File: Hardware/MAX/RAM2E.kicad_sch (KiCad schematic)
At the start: 61 parts, among them J1 AppleIIeAux, J2 JTAG, J3 C14M, U1 EPM240T100, U2 W9812G6KH-6, U3 74LVC245APW, U4 74LVC245APW, U5 74LVC245APW, U6 74AHCT245PW, U7 74AHCT245PW, U8 XC6206P332MR, U9 AP2127K-1.8TRG1

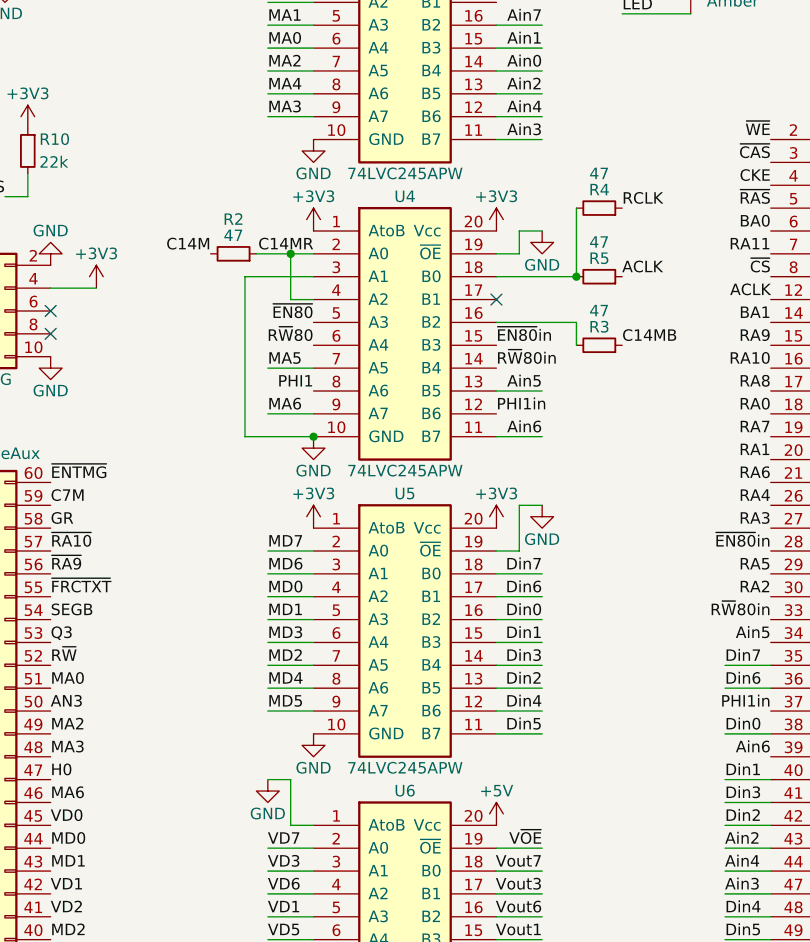
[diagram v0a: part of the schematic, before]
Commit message: Change BOM to separate U4 from U3 and U5
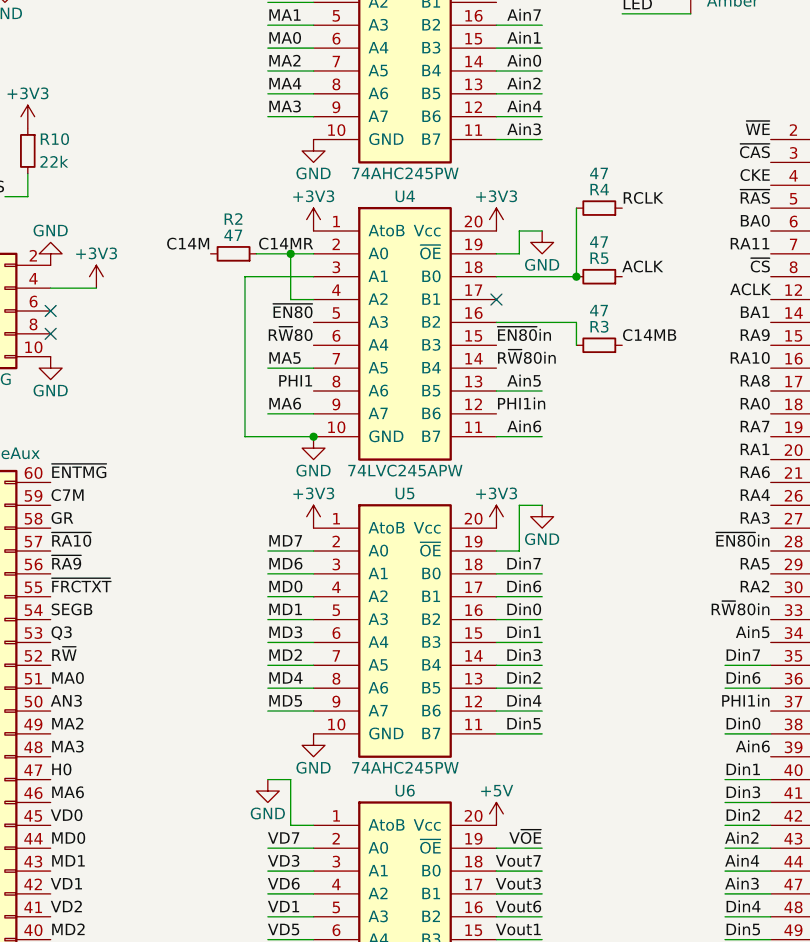
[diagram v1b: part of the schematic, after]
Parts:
- U3, U5: value 74LVC245APW -> 74AHC245PW; LCSC Part C6082 -> C5516
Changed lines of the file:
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@@
       (effects (font (size 1.27 1.27)))
     )
-    (property "Value" "74LVC245APW" (at 76.2 53.34 0)
+    (property "Value" "74AHC245PW" (at 76.2 53.34 0)
       (effects (font (size 1.27 1.27)))
     )
@@
       (effects (font (size 1.524 1.524)) hide)
     )
-    (property "LCSC Part" "C6082" (at 76.2 38.1 0)
+    (property "LCSC Part" "C5516" (at 76.2 38.1 0)
       (effects (font (size 1.27 1.27)) hide)
     )
@@
       (effects (font (size 1.27 1.27)))
     )
-    (property "Value" "74LVC245APW" (at 76.2 119.38 0)
+    (property "Value" "74AHC245PW" (at 76.2 119.38 0)
       (effects (font (size 1.27 1.27)))
     )
@@
       (effects (font (size 1.524 1.524)) hide)
     )
-    (property "LCSC Part" "C6082" (at 76.2 104.14 0)
+    (property "LCSC Part" "C5516" (at 76.2 104.14 0)
       (effects (font (size 1.27 1.27)) hide)
     )

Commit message: RC 2.1
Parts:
- removed J2: JTAG, stdpads:TC2050, symbol Connector_Generic:Conn_02x05_Odd_Even
- added C30, C31, C32: 22p, stdpads:C_0603, symbol Device:C_Small
- added C33, C34, C35, C36: 2u2, stdpads:C_0603, symbol Device:C_Small
- added J2: microUSB, stdpads:USB_Micro-B_Amphenol_10118192-0001, symbol Connector:USB_B_Micro
- added J3: C14M, stdpads:EdgeClipHole, symbol Connector_Generic:Conn_01x01
- added J5: JTAG, stdpads:Tag-Connect_TC2050-IDC-FP_2x05_P1.27mm_Vertical, symbol Connector_Generic:Conn_02x05_Odd_Even
- added R13: 47, stdpads:R_0603, symbol Device:R_Small
- added U10: CH340G, stdpads:SOIC-16_3.9mm, symbol Interface_USB:CH340G
- added U11: 74AHCT1G125GW, stdpads:SOT-353, symbol GW_Logic:741G125GW
- added Y1: 12M, stdpads:Crystal_SMD_3225-4Pin_3.2x2.5mm, symbol Device:Crystal_GND24_Small
- C1, C2, C29, C3, C4, C5, C6: Mfg. Part Numbers Samsung CL21A106KAYNNNE -> (none); Notes 10V or higher. Any manufacturer's part is acceptable but Sa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 -> (none)
- C10, C11, C12, C13, C14, C15, C16, C17, C18, C19, C20, C21, C22, C23, C24, C25, C26, C27, C28, C7, C8, C9: Mfg. Part Numbers Samsung CL10A225KO8NNNC -> (none); Notes 10V or higher. Any manufacturer's part is acceptable but Sa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 -> (none)
- D1: LCSC Part (none) -> C284932; Notes Any manufacturer's part is acceptable. -> (none)
- FID1, FID2, FID3, FID4: Notes DNP - SMT vision system fiducial -> (none)
- H1, H2, H3, H4: Notes DNP - mounting hole for solder paste printing -> (none)
- H5: Notes DNP - mounting hole -> (none)
- J1: Notes DNP - edge connector -> (none)
- J4: renamed from J3; footprint Connector_PinHeader_2.54mm:PinHeader_1x02_P2.54mm_Vertical -> stdpads:PinHeader_1x02_P2.54mm_Vertical; Notes DNP -> (none)
- R1: Mfg. Part Numbers Uniroyal 0805W8F0000T5E -> (none); Notes Any manufacturer's part is acceptable. -> (none)
- R10: value 22k -> DNP; footprint stdpads:R_0805 -> stdpads:R_0603; LCSC Part C17560 -> (none); Mfg. Part Numbers Uniroyal 0805W8F2202T5E -> (none); Notes Any manufacturer's part is acceptable. -> (none)
- R2, R3, R4, R5: Mfg. Part Numbers Uniroyal 0603WAF470JT5E -> (none); Notes Any manufacturer's part is acceptable. -> (none)
- R6: value 0 -> DNP; footprint stdpads:R_0805 -> stdpads:R_0603; LCSC Part C17477 -> (none); Mfg. Part Numbers Uniroyal 0805W8F0000T5E -> (none); Notes Any manufacturer's part is acceptable. -> (none)
- R7: footprint stdpads:R_0805 -> stdpads:R_0603
- R8: Mfg. Part Numbers Uniroyal 0805W8F2200T5E -> (none); Notes Any manufacturer's part is acceptable. -> (none)
- R9: value 22k -> 10k; footprint stdpads:R_0805 -> stdpads:R_0603; LCSC Part C17560 -> C25804; Mfg. Part Numbers Uniroyal 0805W8F2202T5E -> (none); Notes Any manufacturer's part is acceptable. -> (none)
- U1: value EPM240T100 -> 5M240ZT100C5N; LCSC Part C10041 -> C192889; Mfg. Part Numbers Altera 5M240ZT100C5N, Altera 5M240ZT100C4N, Altera 5M240ZT1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 -> (none)
- U2: Mfg. Part Numbers Winbond W9812G6KH-6, Winbond W9812G6KH-6I, Winbond W9825G6K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 -> (none); Notes Most 166 MHz 128/256 Mbit x16 SDRAM is acceptable. -> (none)
- U3, U4, U5: Mfg. Part Numbers NXP 74LVC245APW, TI SN74LVC245APW, NXP 74AHC245PW, NXP 74AH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 -> (none); Notes Most 74LVC245 or 74AHC245 in TSSOP-20 package is acceptable. -> (none)
- U6, U7: Mfg. Part Numbers NXP 74AHCT245PW, NXP 74AHCT245APW, TI SN74AHCT245PW -> (none); Notes Most 74AHCT245 in TSSOP-20 package is acceptable. -> (none)
- U8: Mfg. Part Numbers Torex XC6206P332MR -> (none); Notes Most 3.3V regulator in SOT-23 package is acceptable. -> (none)
- U9: Mfg. Part Numbers Diodes AP2127K-1.8TRG1, Torex XC6228D182VR -> (none); Notes Most 1.8V regulator in SOT-23-5 package is acceptable. -> (none)
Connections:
- net +3V3: now also R6.1, R9.1, C34.1, C35.1, J5.4 (Pin_4), U10.10 (~{DSR}), U10.11 (~{RI}), U10.16 (VCC), U10.3 (RXD), U10.4 (V3); no longer R10.1
- net +5V: now also C36.1, U11.5 (Vcc)
- net AN3: now also U11.2 (A); no longer R6.2, R7.2
- net C14MB: now also J3.1 (Pin_1)
- net GND: now also R7.2, C30.2, C31.2, C32.2, C33.2, C34.2, C35.2, C36.2, J2.5 (GND), J2.6 (Shield), J5.10 (Pin_10), J5.2 (Pin_2), U10.1 (GND), U10.12 (~{DCD}), U10.15 (R232), U11.3 (GND), Y1.2, Y1.4; no longer R9.2
- net R~{W}: now also U3.3 (A1); no longer U3.2 (A0)
- net R~{W}in: now also U3.17 (B1); no longer U3.18 (B0)
- net TCK: now also R10.1, R7.1, C30.1, R13.2; no longer R9.1
- net TDI: now also J5.9 (Pin_9), U10.13 (~{DTR})
- net TDO: now also J5.3 (Pin_3), U10.9 (~{CTS})
- net TMS: now also R6.2, J5.5 (Pin_5), U10.14 (~{RTS}); no longer R10.2
- net ~{C07X}: now also U3.2 (A0); no longer U3.3 (A1)
- net ~{C07X}in: now also U3.18 (B0); no longer U3.17 (B1)
- net ~{FRCTXT}: now also U11.4 (Y); no longer R6.1, R7.1
- net DHGR~{OE}: now reaches U1.87 (IO2_87)
- net DHGR~{OE}: now also R9.2, U11.1 (~{OE})
- new net: C31.1, U10.8 (XO), Y1.3
- new net: J2.2 (D-), U10.6 (UD-)
- new net: J2.3 (D+), U10.5 (UD+)
- new net: C32.1, U10.7 (XI), Y1.1
- new net TCKr: J5.1 (Pin_1), R10.2
- new net USB5V: C33.1, J2.1 (VBUS)
- new net UTCK: R13.1, U10.2 (TXD)
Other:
- moved on the sheet: C16, C19, C29, D1, FID1, FID2, FID3, FID4, H1, H2, H3, H4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

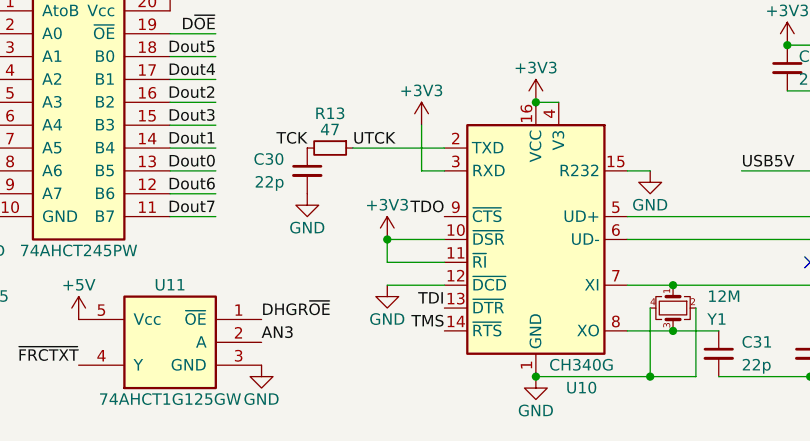
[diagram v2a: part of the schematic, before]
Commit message: RC
Fix board IDs
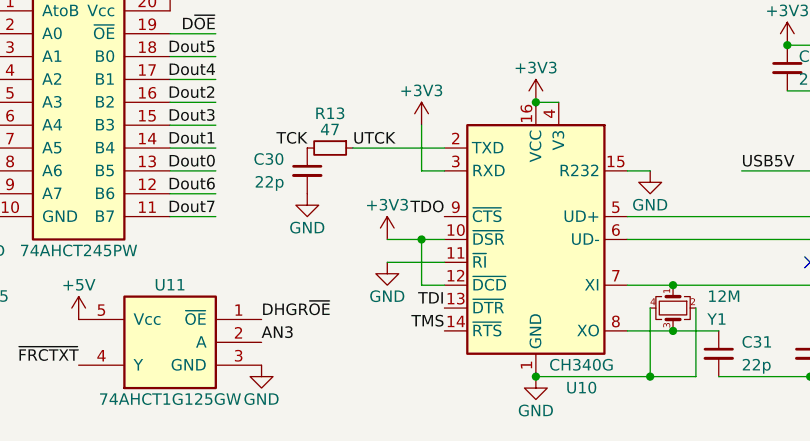
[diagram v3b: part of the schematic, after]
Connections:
- net +3V3: now also U10.12 (~{DCD}); no longer U10.11 (~{RI})
- net GND: now also U10.11 (~{RI}); no longer U10.12 (~{DCD})
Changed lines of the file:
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@@
   (junction (at 80.01 62.23) (diameter 0) (color 0 0 0 0)
   )
-  (junction (at 95.25 181.61) (diameter 0) (color 0 0 0 0)
-  )
   (junction (at 218.44 19.05) (diameter 0) (color 0 0 0 0)
   )
@@
   (junction (at 130.81 21.59) (diameter 0) (color 0 0 0 0)
   )
+  (junction (at 99.06 181.61) (diameter 0) (color 0 0 0 0)
+  )
   (junction (at 187.96 19.05) (diameter 0) (color 0 0 0 0)
   )
@@
     (stroke (width 0) (type default))
   )
+  (wire (pts (xy 95.25 181.61) (xy 99.06 181.61))
+    (stroke (width 0) (type default))
+  )
   (wire (pts (xy 45.72 72.39) (xy 50.8 72.39))
     (stroke (width 0) (type default))
@@
     (stroke (width 0) (type default))
   )
-  (wire (pts (xy 95.25 184.15) (xy 95.25 181.61))
-    (stroke (width 0) (type default))
-  )
   (wire (pts (xy 48.26 64.77) (xy 50.8 64.77))
     (stroke (width 0) (type default))
@@
     (stroke (width 0) (type default))
   )
+  (wire (pts (xy 101.6 186.69) (xy 99.06 186.69))
+    (stroke (width 0) (type default))
+  )
   (wire (pts (xy 73.66 87.63) (xy 76.2 87.63))
     (stroke (width 0) (type default))
@@
     (stroke (width 0) (type default))
   )
-  (wire (pts (xy 95.25 186.69) (xy 101.6 186.69))
-    (stroke (width 0) (type default))
-  )
   (wire (pts (xy 246.38 120.65) (xy 241.3 120.65))
     (stroke (width 0) (type default))
@@
     (stroke (width 0) (type default))
   )
+  (wire (pts (xy 101.6 184.15) (xy 95.25 184.15))
+    (stroke (width 0) (type default))
+  )
   (wire (pts (xy 208.28 64.77) (xy 218.44 64.77))
     (stroke (width 0) (type default))
@@
     (stroke (width 0) (type default))
   )
+  (wire (pts (xy 99.06 186.69) (xy 99.06 181.61))
+    (stroke (width 0) (type default))
+  )
   (bus (pts (xy 208.28 140.97) (xy 208.28 143.51))
     (stroke (width 0) (type default))
@@
     (stroke (width 0) (type default))
   )
-  (wire (pts (xy 246.38 115.57) (xy 241.3 115.57))
+  (wire (pts (xy 99.06 181.61) (xy 101.6 181.61))
     (stroke (width 0) (type default))
   )
-  (wire (pts (xy 215.9 118.11) (xy 210.82 118.11))
+  (wire (pts (xy 246.38 115.57) (xy 241.3 115.57))
     (stroke (width 0) (type default))
   )
-  (wire (pts (xy 95.25 181.61) (xy 101.6 181.61))
+  (wire (pts (xy 215.9 118.11) (xy 210.82 118.11))
     (stroke (width 0) (type default))
   )
@@
     (stroke (width 0) (type default))
   )
-  (wire (pts (xy 101.6 184.15) (xy 95.25 184.15))
-    (stroke (width 0) (type default))
-  )
   (wire (pts (xy 187.96 34.29) (xy 187.96 36.83))
     (stroke (width 0) (type default))
@@
     )
   )
-  (symbol (lib_id "power:+3V3") (at 95.25 181.61 0) (mirror y) (unit 1)
-    (in_bom yes) (on_board yes) (dnp no)
-    (property "Reference" "#PWR05" (at 95.25 185.42 0)
-      (effects (font (size 1.27 1.27)) hide)
-    )
-    (property "Value" "+3V3" (at 95.25 177.8 0)
-      (effects (font (size 1.27 1.27)))
-    )
-    (property "Footprint" "" (at 95.25 181.61 0)
-      (effects (font (size 1.27 1.27)) hide)
-    )
-    (property "Datasheet" "" (at 95.25 181.61 0)
-      (effects (font (size 1.27 1.27)) hide)
-    )
-    (pin "1")
-    (instances
-      (project "RAM2E"
-        (path "/0dd11af3-0465-4c84-bbb0-f3ae16a77316"
-          (reference "#PWR05") (unit 1)
-        )
-      )
-    )
-  )
   (symbol (lib_id "Connector:USB_B_Micro") (at 149.86 179.07 0) (mirror y) (unit 1)
     (in_bom yes) (on_board yes) (dnp no)
@@
     )
   )
+  (symbol (lib_id "power:GND") (at 95.25 184.15 0) (mirror y) (unit 1)
+    (in_bom yes) (on_board yes) (dnp no)
+    (property "Reference" "#PWR06" (at 95.25 190.5 0)
+      (effects (font (size 1.27 1.27)) hide)
+    )
+    (property "Value" "GND" (at 95.25 187.96 0)
+      (effects (font (size 1.27 1.27)))
+    )
+    (property "Footprint" "" (at 95.25 184.15 0)
+      (effects (font (size 1.27 1.27)) hide)
+    )
+    (property "Datasheet" "" (at 95.25 184.15 0)
+      (effects (font (size 1.27 1.27)) hide)
+    )
+    (pin "1")
+    (instances
+      (project "RAM2E"
+        (path "/0dd11af3-0465-4c84-bbb0-f3ae16a77316"
+          (reference "#PWR06") (unit 1)
+        )
+      )
+    )
+  )
   (symbol (lib_id "Device:R_Small") (at 88.9 171.45 270) (unit 1)
     (in_bom yes) (on_board yes) (dnp no)
@@
     )
   )
+  (symbol (lib_id "power:+3V3") (at 95.25 181.61 0) (mirror y) (unit 1)
+    (in_bom yes) (on_board yes) (dnp no)
+    (property "Reference" "#PWR05" (at 95.25 185.42 0)
+      (effects (font (size 1.27 1.27)) hide)
+    )
+    (property "Value" "+3V3" (at 95.25 177.8 0)
+      (effects (font (size 1.27 1.27)))
+    )
+    (property "Footprint" "" (at 95.25 181.61 0)
+      (effects (font (size 1.27 1.27)) hide)
+    )
+    (property "Datasheet" "" (at 95.25 181.61 0)
+      (effects (font (size 1.27 1.27)) hide)
+    )
+    (pin "1")
+    (instances
+      (project "RAM2E"
+        (path "/0dd11af3-0465-4c84-bbb0-f3ae16a77316"
+          (reference "#PWR05") (unit 1)
+        )
+      )
+    )
+  )
   (symbol (lib_id "Interface_USB:CH340G") (at 111.76 181.61 0) (mirror y) (unit 1)
     (in_bom yes) (on_board yes) (dnp no)
@@
         )
       )
-    )
-  )
-  (symbol (lib_id "power:GND") (at 95.25 186.69 0) (mirror y) (unit 1)
-    (in_bom yes) (on_board yes) (dnp no)
-    (property "Reference" "#PWR06" (at 95.25 193.04 0)
-      (effects (font (size 1.27 1.27)) hide)
-    )
-    (property "Value" "GND" (at 95.25 190.5 0)
-      (effects (font (size 1.27 1.27)))
-    )
-    (property "Footprint" "" (at 95.25 186.69 0)
-      (effects (font (size 1.27 1.27)) hide)
-    )
-    (property "Datasheet" "" (at 95.25 186.69 0)
-      (effects (font (size 1.27 1.27)) hide)
-    )
-    (pin "1")
-    (instances
-      (project "RAM2E"
-        (path "/0dd11af3-0465-4c84-bbb0-f3ae16a77316"
-          (reference "#PWR06") (unit 1)
-        )
-      )

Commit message: RC
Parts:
- added R11, R12: 10k, stdpads:R_0603, symbol Device:R_Small
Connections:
- net +3V3: now also R11.1, R12.1
- net D~{OE}: now also R12.2
- net V~{OE}: now also R11.2
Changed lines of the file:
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@@
   (junction (at 228.6 49.53) (diameter 0) (color 0 0 0 0)
   )
+  (junction (at 104.14 144.78) (diameter 0) (color 0 0 0 0)
+  )
   (junction (at 228.6 29.21) (diameter 0) (color 0 0 0 0)
   )
@@
     (stroke (width 0) (type default))
   )
+  (wire (pts (xy 96.52 151.13) (xy 104.14 151.13))
+    (stroke (width 0) (type default))
+  )
   (wire (pts (xy 171.45 85.09) (xy 166.37 85.09))
     (stroke (width 0) (type default))
@@
     (stroke (width 0) (type default))
   )
+  (wire (pts (xy 104.14 149.86) (xy 104.14 151.13))
+    (stroke (width 0) (type default))
+  )
   (wire (pts (xy 215.9 138.43) (xy 210.82 138.43))
     (stroke (width 0) (type default))
@@
     (stroke (width 0) (type default))
   )
+  (wire (pts (xy 104.14 144.78) (xy 111.76 144.78))
+    (stroke (width 0) (type default))
+  )
   (wire (pts (xy 228.6 34.29) (xy 218.44 34.29))
     (stroke (width 0) (type default))
@@
     (stroke (width 0) (type default))
   )
+  (wire (pts (xy 111.76 149.86) (xy 111.76 153.67))
+    (stroke (width 0) (type default))
+  )
   (wire (pts (xy 215.9 120.65) (xy 210.82 120.65))
     (stroke (width 0) (type default))
@@
     (stroke (width 0) (type default))
   )
+  (wire (pts (xy 96.52 153.67) (xy 111.76 153.67))
+    (stroke (width 0) (type default))
+  )
   (bus (pts (xy 208.28 110.49) (xy 208.28 113.03))
     (stroke (width 0) (type default))
@@
     (effects (font (size 1.27 1.27)) (justify right bottom))
   )
+  (label "D~{OE}" (at 96.52 153.67 0) (fields_autoplaced)
+    (effects (font (size 1.27 1.27)) (justify left bottom))
+  )
   (label "TDI" (at 21.59 88.9 180) (fields_autoplaced)
     (effects (font (size 1.27 1.27)) (justify right bottom))
@@
     (effects (font (size 1.27 1.27)) (justify right bottom))
   )
+  (label "V~{OE}" (at 96.52 151.13 0) (fields_autoplaced)
+    (effects (font (size 1.27 1.27)) (justify left bottom))
+  )
   (label "Ain5" (at 115.57 85.09 180) (fields_autoplaced)
     (effects (font (size 1.27 1.27)) (justify right bottom))
@@
     )
   )
+  (symbol (lib_id "Device:R_Small") (at 104.14 147.32 0) (unit 1)
+    (in_bom yes) (on_board yes) (dnp no)
+    (property "Reference" "R11" (at 105.41 146.05 0)
+      (effects (font (size 1.27 1.27)) (justify left))
+    )
+    (property "Value" "10k" (at 105.41 148.59 0)
+      (effects (font (size 1.27 1.27)) (justify left))
+    )
+    (property "Footprint" "stdpads:R_0603" (at 104.14 147.32 0)
+      (effects (font (size 1.27 1.27)) hide)
+    )
+    (property "Datasheet" "~" (at 104.14 147.32 0)
+      (effects (font (size 1.27 1.27)) hide)
+    )
+    (property "LCSC Part" "C25804" (at 104.14 147.32 0)
+      (effects (font (size 1.27 1.27)) hide)
+    )
+    (pin "1")
+    (pin "2")
+    (instances
+      (project "RAM2E"
+        (path "/0dd11af3-0465-4c84-bbb0-f3ae16a77316"
+          (reference "R11") (unit 1)
+        )
+      )
+    )
+  )
   (symbol (lib_id "power:+5V") (at 60.96 190.5 0) (unit 1)
     (in_bom yes) (on_board yes) (dnp no)
@@
     )
   )
+  (symbol (lib_id "power:+3V3") (at 104.14 144.78 0) (mirror y) (unit 1)
+    (in_bom yes) (on_board yes) (dnp no)
+    (property "Reference" "#PWR016" (at 104.14 148.59 0)
+      (effects (font (size 1.27 1.27)) hide)
+    )
+    (property "Value" "+3V3" (at 104.14 140.97 0)
+      (effects (font (size 1.27 1.27)))
+    )
+    (property "Footprint" "" (at 104.14 144.78 0)
+      (effects (font (size 1.27 1.27)) hide)
+    )
+    (property "Datasheet" "" (at 104.14 144.78 0)
+      (effects (font (size 1.27 1.27)) hide)
+    )
+    (pin "1")
+    (instances
+      (project "RAM2E"
+        (path "/0dd11af3-0465-4c84-bbb0-f3ae16a77316"
+          (reference "#PWR016") (unit 1)
+        )
+      )
+    )
+  )
   (symbol (lib_id "Connector_Generic:Conn_01x01") (at 26.67 17.78 0) (mirror y) (unit 1)
     (in_bom yes) (on_board yes) (dnp no)
@@
         )
       )
+    )
+  )
+  (symbol (lib_id "Device:R_Small") (at 111.76 147.32 0) (unit 1)
+    (in_bom yes) (on_board yes) (dnp no)
+    (property "Reference" "R12" (at 113.03 146.05 0)
+      (effects (font (size 1.27 1.27)) (justify left))
+    )
+    (property "Value" "10k" (at 113.03 148.59 0)
+      (effects (font (size 1.27 1.27)) (justify left))
+    )
+    (property "Footprint" "stdpads:R_0603" (at 111.76 147.32 0)
+      (effects (font (size 1.27 1.27)) hide)
+    )
+    (property "Datasheet" "~" (at 111.76 147.32 0)
+      (effects (font (size 1.27 1.27)) hide)
+    )
+    (property "LCSC Part" "C25804" (at 111.76 147.32 0)
+      (effects (font (size 1.27 1.27)) hide)
+    )
+    (pin "1")
+    (pin "2")
+    (instances
+      (project "RAM2E"
+        (path "/0dd11af3-0465-4c84-bbb0-f3ae16a77316"
+          (reference "R12") (unit 1)
+        )
+      )

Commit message: RC
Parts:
- U3, U5: value 74AHC245PW -> 74LVC245APW; LCSC Part C5516 -> C6082
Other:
- title: GW4203B (RAM2E II) - EPM240 / 5M240Z / AG256 -> GW4203C (RAM2E II) - EPM240 / 5M240Z / AG256
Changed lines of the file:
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@@
   (paper "USLetter")
   (title_block
-    (title "GW4203B (RAM2E II) - EPM240 / 5M240Z / AG256")
-    (date "2024-04-24")
-    (rev "2.1")
+    (title "GW4203C (RAM2E II) - EPM240 / 5M240Z / AG256")
+    (date "2024-05-20")
+    (rev "1.0")
     (company "Garrett's Workshop")
   )
@@
       (effects (font (size 1.27 1.27)))
     )
-    (property "Value" "74AHC245PW" (at 60.96 50.8 0)
+    (property "Value" "74LVC245APW" (at 60.96 50.8 0)
       (effects (font (size 1.27 1.27)))
     )
@@
       (effects (font (size 1.524 1.524)) hide)
     )
-    (property "LCSC Part" "C5516" (at 60.96 35.56 0)
+    (property "LCSC Part" "C6082" (at 60.96 35.56 0)
       (effects (font (size 1.27 1.27)) hide)
     )
@@
       (effects (font (size 1.27 1.27)))
     )
-    (property "Value" "74AHC245PW" (at 60.96 116.84 0)
+    (property "Value" "74LVC245APW" (at 60.96 116.84 0)
       (effects (font (size 1.27 1.27)))
     )
@@
       (effects (font (size 1.524 1.524)) hide)
     )
-    (property "LCSC Part" "C5516" (at 60.96 101.6 0)
-      (effects (font (size 1.27 1.27)) hide)
-    )
+    (property "LCSC Part" "C6082" (at 60.96 101.6 0)
+      (effects (font (size 1.27 1.27)) hide)
+    )
